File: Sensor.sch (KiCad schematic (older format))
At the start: 0 parts

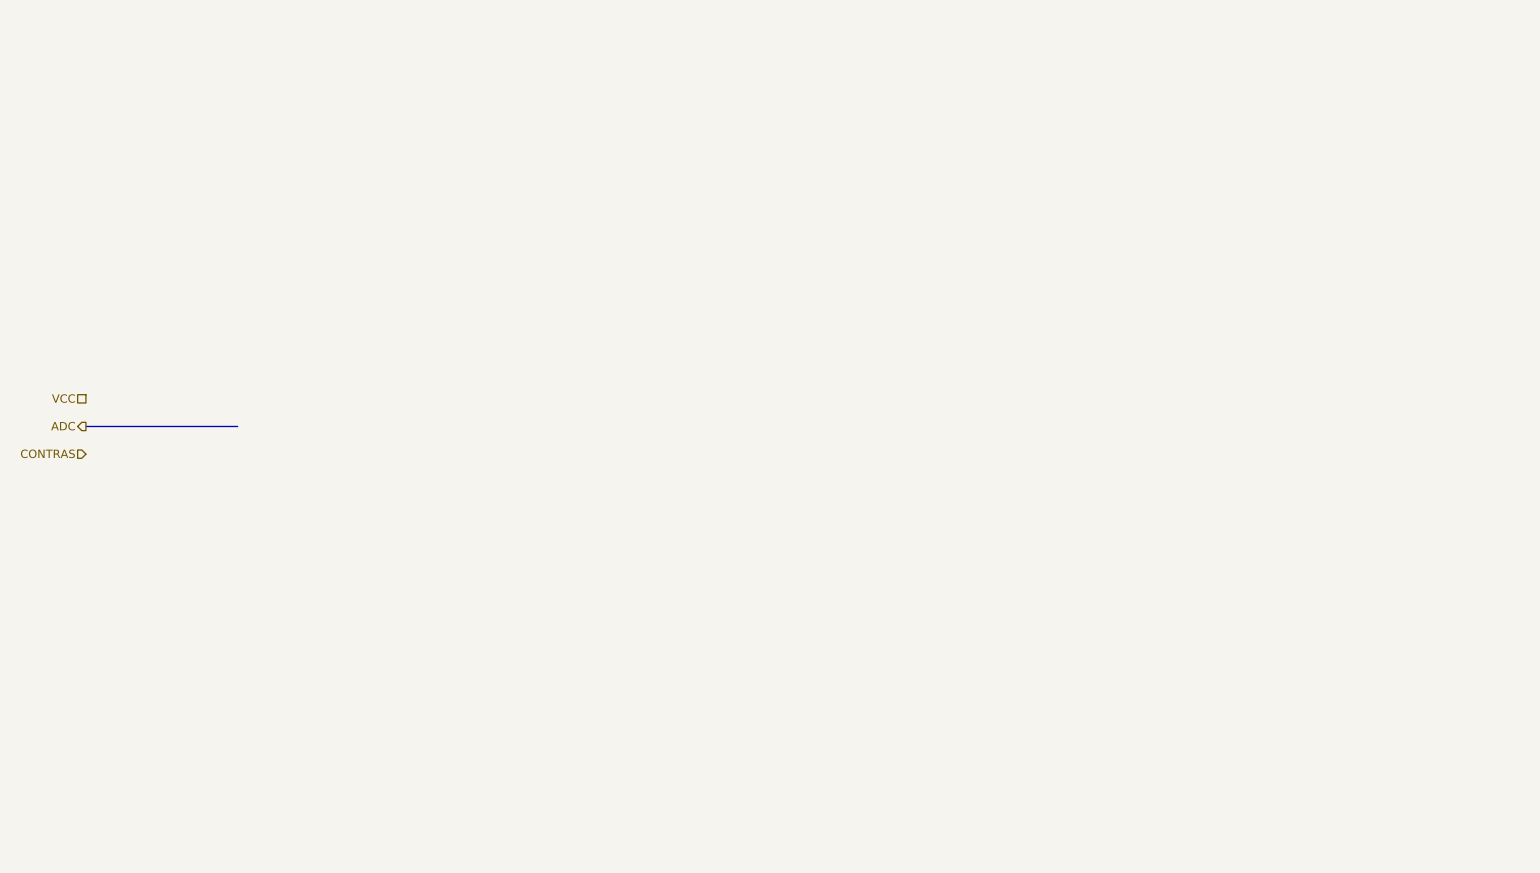
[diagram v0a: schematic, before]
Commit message: Changes to be committed: 	new file:   78LXXSOT89.pdf 	modified:   Control.sch 	modified:   Debugger.sch 	modified:   MotorDriver.sch 	modified:   PS.sch 	modified:   Sensor.sch 	new file:   XL6009-Schematic-Diagram.pdf 	modified:   main-cache.lib 	new file:   main.cmp 	new file:   main.kicad_pcb 	new file:   main.net 	modified:   main.pro 	modified:   main.sch
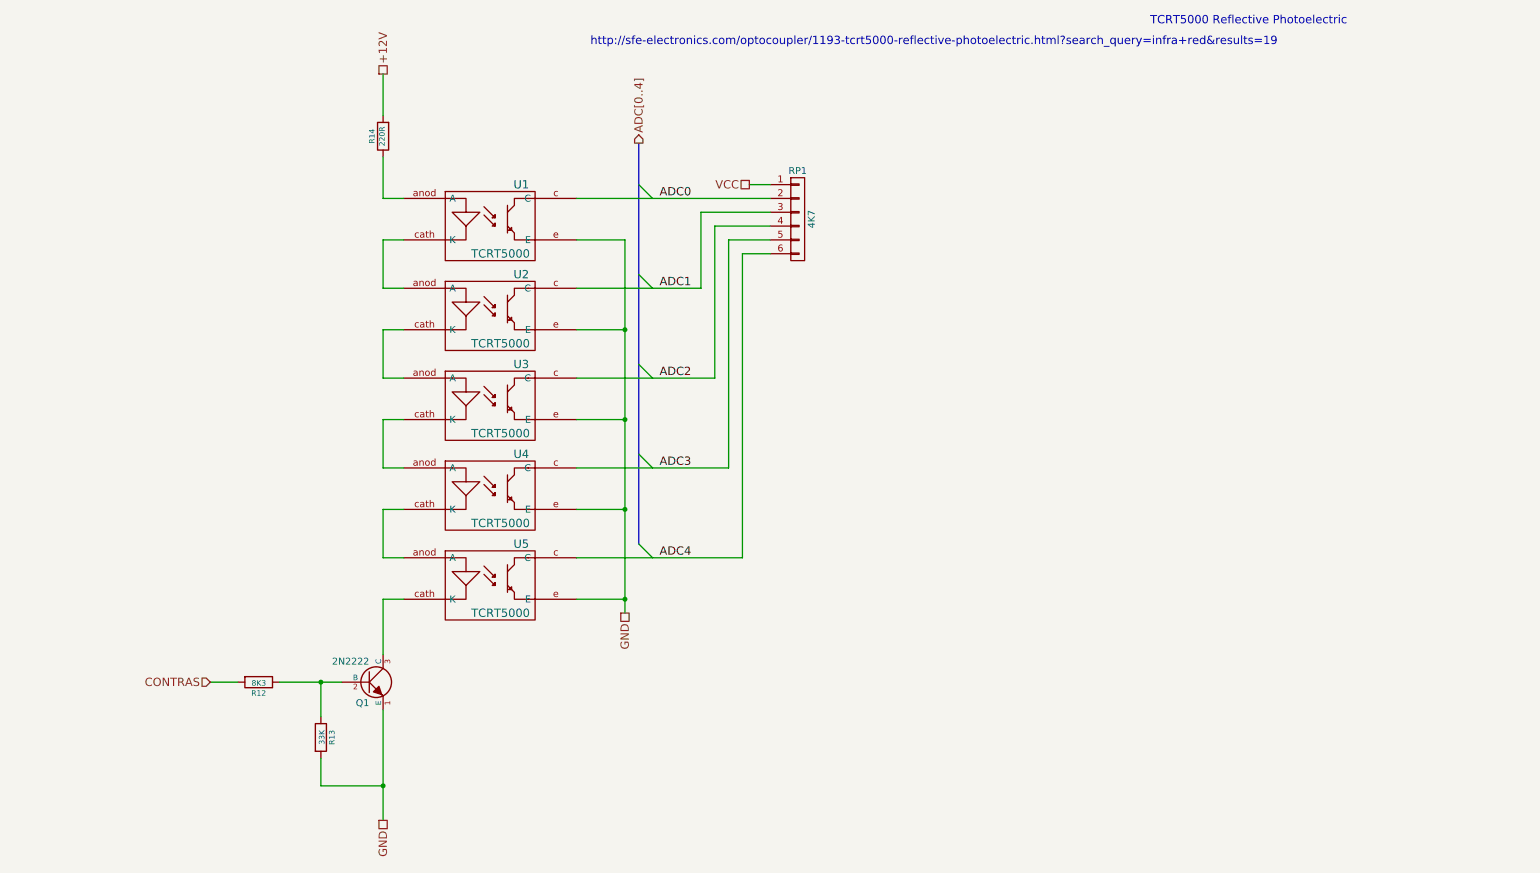
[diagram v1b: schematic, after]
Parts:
- added Q1: 2N2222, Discret:TO92PN, symbol NPN
- added R12: 8K3, Resistors_SMD:R_0805_HandSoldering, symbol R
- added R13: 33K, Resistors_SMD:R_0805_HandSoldering, symbol R
- added R14: 220R, Resistors_SMD:R_0805_HandSoldering, symbol R
- added RP1: 4K7, Pin_Arrays:pin_array_1x06, symbol CONN_01X06
- added U1, U2, U3, U4, U5: TCRT5000, TCRT5000:TCRT5000, symbol TCRT5000
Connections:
- net CONTRAS: now also R12.2
- net VCC: now also RP1.1 (P1)
- new net: R14.1, U1.anod (A)
- new net: U1.cath (K), U2.anod (A)
- new net: U2.cath (K), U3.anod (A)
- new net: U3.cath (K), U4.anod (A)
- new net: U4.cath (K), U5.anod (A)
- new net: Q1.3 (C), U5.cath (K)
- new net: Q1.2 (B), R12.1, R13.1
- new net +12V: R14.2
- new net ADC0: RP1.2 (P2), U1.c (C)
- new net ADC1: RP1.3 (P3), U2.c (C)
- new net ADC2: RP1.4 (P4), U3.c (C)
- new net ADC3: RP1.5 (P5), U4.c (C)
- new net ADC4: RP1.6 (P6), U5.c (C)
- new net GND: Q1.1 (E), R13.2, U1.e (E), U2.e (E), U3.e (E), U4.e (E), U5.e (E)
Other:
- note added: "TCRT5000 Reflective Photoelectric"
- note added: "http://sfe-electronics.com/optocoupler/1193-tcrt5000-reflective-photoelectric.html?search_query=infra+red&results=19"

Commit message: update
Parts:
- removed Q1: 2N2222, Discret:TO92PN, symbol NPN
- removed R12: 8K3, Resistors_SMD:R_0805_HandSoldering, symbol R
- removed R13: 33K, Resistors_SMD:R_0805_HandSoldering, symbol R
- removed R14: 220R, Resistors_SMD:R_0805_HandSoldering, symbol R
- removed RP1: 4K7, Pin_Arrays:pin_array_1x06, symbol CONN_01X06
- removed U1, U2, U3, U4, U5: TCRT5000, TCRT5000:TCRT5000, symbol TCRT5000
- added P6: SENSOR, Pin_Headers:Pin_Header_Straight_1x09, symbol CONN_01X09
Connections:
- net +12V: now also P6.3 (P3)
- net ADC0: now also P6.8 (P8)
- net ADC1: now also P6.7 (P7)
- net ADC2: now also P6.6 (P6)
- net ADC3: now also P6.5 (P5)
- net ADC4: now also P6.4 (P4)
- net CONTRAS: now also P6.9 (P9)
- net GND: now also P6.1 (P1)
- net VCC: now also P6.2 (P2)
